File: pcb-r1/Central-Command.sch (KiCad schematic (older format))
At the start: 12 parts, among them P101 CONN_01X10, P102 CONN_01X10, P103 CONN_01X04, P104 CONN_01X02, P105 CONN_01X04, P106 CONN_01X02, U101 STM32F030C8, Y101 Crystal

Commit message: Started preliminary layout of the parts
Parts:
- C102, C103: footprint (none) -> Capacitors_SMD:C_0805
- P101, P102: footprint (none) -> Pin_Headers:Pin_Header_Straight_1x10
- P103, P105: footprint (none) -> Pin_Headers:Pin_Header_Straight_1x04
- P104, P106: footprint (none) -> Pin_Headers:Pin_Header_Straight_1x02
- Y101: footprint (none) -> Crystals:Crystal_HC49-U_Vertical
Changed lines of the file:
@@
 F 0 "Y101" H 4650 1900 50  0000 C CNN
 F 1 "Crystal" H 4650 1600 50  0000 C CNN
-F 2 "" H 4650 1750 60  0001 C CNN
+F 2 "Crystals:Crystal_HC49-U_Vertical" H 4650 1750 60  0001 C CNN
 F 3 "" H 4650 1750 60  0000 C CNN
 F 4 "http://parts.io/detail/343558/FOXSLF%2F080-20" H 4650 1750 60  0001 C CNN "Link"
@@
 F 0 "C103" V 5400 2000 50  0000 L CNN
 F 1 "20pF" V 5100 2000 50  0000 L CNN
-F 2 "" H 5288 1850 30  0001 C CNN
+F 2 "Capacitors_SMD:C_0805" H 5288 1850 30  0001 C CNN
 F 3 "" H 5250 2000 60  0000 C CNN
 	1    5250 2000
@@
 F 0 "C102" V 5400 1550 50  0000 L CNN
 F 1 "20pF" V 5100 1550 50  0000 L CNN
-F 2 "" H 5288 1400 30  0001 C CNN
+F 2 "Capacitors_SMD:C_0805" H 5288 1400 30  0001 C CNN
 F 3 "" H 5250 1550 60  0000 C CNN
 	1    5250 1550
@@
 F 0 "P101" H 700 5650 50  0000 C CNN
 F 1 "CONN_01X10" V 800 5100 50  0001 C CNN
-F 2 "" H 700 5100 60  0001 C CNN
+F 2 "Pin_Headers:Pin_Header_Straight_1x10" H 700 5100 60  0001 C CNN
 F 3 "" H 700 5100 60  0000 C CNN
 	1    700  5100
@@
 F 0 "P102" H 850 2700 50  0000 C CNN
 F 1 "CONN_01X10" V 950 2150 50  0001 C CNN
-F 2 "" H 850 2150 60  0001 C CNN
+F 2 "Pin_Headers:Pin_Header_Straight_1x10" H 850 2150 60  0001 C CNN
 F 3 "" H 850 2150 60  0000 C CNN
 	1    850  2150
@@
 F 0 "P105" H 5200 3500 50  0000 C CNN
 F 1 "CONN_01X04" V 5300 3250 50  0001 C CNN
-F 2 "" H 5200 3250 60  0001 C CNN
+F 2 "Pin_Headers:Pin_Header_Straight_1x04" H 5200 3250 60  0001 C CNN
 F 3 "" H 5200 3250 60  0000 C CNN
 	1    5200 3250
@@
 F 0 "P103" H 4950 4950 50  0000 C CNN
 F 1 "CONN_01X04" V 5050 4700 50  0001 C CNN
-F 2 "" H 4950 4700 60  0001 C CNN
+F 2 "Pin_Headers:Pin_Header_Straight_1x04" H 4950 4700 60  0001 C CNN
 F 3 "" H 4950 4700 60  0000 C CNN
 	1    4950 4700
@@
 F 0 "P106" H 6400 4850 50  0000 C CNN
 F 1 "CONN_01X02" V 6500 4700 50  0001 C CNN
-F 2 "" H 6400 4700 60  0001 C CNN
+F 2 "Pin_Headers:Pin_Header_Straight_1x02" H 6400 4700 60  0001 C CNN
 F 3 "" H 6400 4700 60  0000 C CNN
 	1    6400 4700
@@
 F 0 "P104" H 5000 6000 50  0000 C CNN
 F 1 "CONN_01X02" V 5100 5850 50  0001 C CNN
-F 2 "" H 5000 5850 60  0001 C CNN
+F 2 "Pin_Headers:Pin_Header_Straight_1x02" H 5000 5850 60  0001 C CNN
 F 3 "" H 5000 5850 60  0000 C CNN
 	1    5000 5850

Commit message: New initial layout
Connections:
- net 3V3 is gone; now on net PWR: L101.1, U101.1 (VDD), U101.24 (VDD), U101.48 (VDD)
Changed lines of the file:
@@
 	1    0    0    -1
 $EndComp
-Text GLabel 2500 900  0    60   Input ~ 0
-3V3
 Text Notes 4500 1250 0    60   ~ 0
 TODO: Get crystal/oscillator
@@
 Connection ~ 2900 3250
 Wire Wire Line
-	2500 900  2900 900
+	2250 900  2900 900
 Wire Wire Line
 	2900 800  2900 1000
@@
 Wire Wire Line
 	9450 4750 9450 5050
+Text Label 2250 900  0    60   ~ 0
+PWR
 $EndSCHEMATC

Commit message: Intermediate save of the layout
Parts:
- added C104, C107: 0.1μF, Capacitors_SMD:C_0805, symbol C
- added C105, C108: 1μF, Capacitors_SMD:C_1206, symbol C
- added C106, C109: 10μF, Capacitors_SMD:C_1206, symbol C
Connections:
- net I2C1_SLK is gone; now on net I2C1_SCK: U101.36 (PF7/I2C1_SCK)
- net GND: now also C104.1, C105.1, C106.1, C107.1, C108.1, C109.1
- net PWR: now also C104.2, C105.2, C106.2, C107.2, C108.2, C109.2
- net I2C1_SCL renamed I2C1_SCK
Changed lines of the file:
@@
 $EndComp
 $Sheet
-S 8550 1450 800  2400
+S 8550 2550 800  2400
 U 56673ABF
 F0 "Comm" 60
 F1 "Comm.sch" 60
-F2 "SWIO" I L 8550 2600 60
-F3 "SWCLK" I L 8550 2750 60
-F4 "TRACE" I L 8550 3050 60
-F5 "NRST" I L 8550 2900 60
-F6 "GND" I L 8550 1800 60
-F7 "PWR" I L 8550 1650 60
-F8 "SCL" I L 8550 2100 60
-F9 "SDA" I L 8550 2250 60
-F10 "BOOT0" I L 8550 3700 60
-F11 "MCO" I L 8550 3400 60
+F2 "SWIO" I L 8550 3700 60
+F3 "SWCLK" I L 8550 3850 60
+F4 "TRACE" I L 8550 4150 60
+F5 "NRST" I L 8550 4000 60
+F6 "GND" I L 8550 2900 60
+F7 "PWR" I L 8550 2750 60
+F8 "SCL" I L 8550 3200 60
+F9 "SDA" I L 8550 3350 60
+F10 "BOOT0" I L 8550 4800 60
+F11 "MCO" I L 8550 4500 60
 $EndSheet
-Text Label 8100 1650 0    60   ~ 0
+Text Label 8100 2750 0    60   ~ 0
 PWR
-Text Label 8100 2100 0    60   ~ 0
+Text Label 8100 3200 0    60   ~ 0
 I2C_SCL
-Text Label 8100 2250 0    60   ~ 0
+Text Label 8100 3350 0    60   ~ 0
 I2C_SDA
-Text Label 8100 2600 0    60   ~ 0
+Text Label 8100 3700 0    60   ~ 0
 SWIO
-Text Label 8100 2750 0    60   ~ 0
+Text Label 8100 3850 0    60   ~ 0
 SWCLK
-Text Label 8100 2900 0    60   ~ 0
+Text Label 8100 4000 0    60   ~ 0
 NRST
-Text Label 8100 3400 0    60   ~ 0
+Text Label 8100 4500 0    60   ~ 0
 MCO
-Text Label 8100 3700 0    60   ~ 0
+Text Label 8100 4800 0    60   ~ 0
 BOOT0
 $Sheet
-S 8250 4350 750  700
+S 8250 5450 750  700
 U 5657EAAA
 F0 "Power" 60
 F1 "Power.sch" 60
-F2 "TXD" I L 8250 4550 60
-F3 "RXD" I L 8250 4750 60
-F4 "PWR" I R 9000 4550 60
-F5 "GND" I R 9000 4750 60
+F2 "TXD" I L 8250 5650 60
+F3 "RXD" I L 8250 5850 60
+F4 "PWR" I R 9000 5650 60
+F5 "GND" I R 9000 5850 60
+F6 "NRST" I L 8250 6050 60
 $EndSheet
-Text Label 9350 4550 2    60   ~ 0
+Text Label 9350 5650 2    60   ~ 0
 PWR
 $Comp
@@
 I2C1_SDA
 Text Label 1450 2300 0    60   ~ 0
-I2C1_SLK
+I2C1_SCK
 Text Label 1450 2500 0    60   ~ 0
 BOOT0
@@
 Connection ~ 4650 2000
 Wire Wire Line
-	9000 4550 9350 4550
-Wire Wire Line
-	8550 1650 8100 1650
-Wire Wire Line
-	8550 2100 8100 2100
-Wire Wire Line
-	8550 2250 8100 2250
-Wire Wire Line
-	8550 2600 8100 2600
+	9000 5650 9350 5650
 Wire Wire Line
 	8550 2750 8100 2750
 Wire Wire Line
-	8550 2900 8100 2900
-Wire Wire Line
-	8550 3050 8100 3050
-Wire Wire Line
-	8550 3400 8100 3400
+	8550 3200 8100 3200
+Wire Wire Line
+	8550 3350 8100 3350
 Wire Wire Line
 	8550 3700 8100 3700
+Wire Wire Line
+	8550 3850 8100 3850
+Wire Wire Line
+	8550 4000 8100 4000
+Wire Wire Line
+	8550 4150 8100 4150
+Wire Wire Line
+	8550 4500 8100 4500
+Wire Wire Line
+	8550 4800 8100 4800
 Wire Wire Line
 	900  4650 2100 4650
@@
 I2C1_SDA
 Text Label 5750 5900 2    60   ~ 0
-I2C1_SCL
+I2C1_SCK
 Wire Notes Line
 	4750 5350 5900 5350
@@
 Sensor I2C Header
 Wire Wire Line
-	8250 4550 7600 4550
-Wire Wire Line
-	7600 4750 8250 4750
-Text Label 7600 4550 0    60   ~ 0
+	8250 5650 7600 5650
+Wire Wire Line
+	7600 5850 8250 5850
+Text Label 7600 5650 0    60   ~ 0
 USART2_TX
-Text Label 7600 4750 0    60   ~ 0
+Text Label 7600 5850 0    60   ~ 0
 USART2_RX
 $Comp
@@
 L GND #PWR05
 U 1 1 56673B6E
-P 9450 5050
-F 0 "#PWR05" H 9450 4800 50  0001 C CNN
-F 1 "GND" H 9450 4900 50  0000 C CNN
-F 2 "" H 9450 5050 60  0000 C CNN
-F 3 "" H 9450 5050 60  0000 C CNN
-	1    9450 5050
+P 9450 6150
+F 0 "#PWR05" H 9450 5900 50  0001 C CNN
+F 1 "GND" H 9450 6000 50  0000 C CNN
+F 2 "" H 9450 6150 60  0000 C CNN
+F 3 "" H 9450 6150 60  0000 C CNN
+	1    9450 6150
 	1    0    0    -1
 $EndComp
 Wire Wire Line
-	9000 4750 9450 4750
-Wire Wire Line
-	9450 4750 9450 5050
+	9000 5850 9450 5850
+Wire Wire Line
+	9450 5850 9450 6150
 Text Label 2250 900  0    60   ~ 0
 PWR
+Wire Wire Line
+	8250 6050 7600 6050
+Text Label 7600 6050 0    60   ~ 0
+NRST
+$Comp
+L C C104
+U 1 1 567EB894
+P 6950 1200
+F 0 "C104" H 7000 1100 50  0000 L CNN
+F 1 "0.1μF" H 6700 1300 50  0000 L CNN
+F 2 "Capacitors_SMD:C_0805" H 6988 1050 30  0001 C CNN
+F 3 "" H 6950 1200 60  0000 C CNN
+	1    6950 1200
+	-1   0    0    1
+$EndComp
+$Comp
+L C C105
+U 1 1 567EC046
+P 7400 1200
+F 0 "C105" H 7450 1100 50  0000 L CNN
+F 1 "1μF" H 7150 1300 50  0000 L CNN
+F 2 "Capacitors_SMD:C_1206" H 7438 1050 30  0001 C CNN
+F 3 "" H 7400 1200 60  0000 C CNN
+	1    7400 1200
+	-1   0    0    1
+$EndComp
+$Comp
+L C C106
+U 1 1 567EC191
+P 7800 1200
+F 0 "C106" H 7850 1100 50  0000 L CNN
+F 1 "10μF" H 7550 1300 50  0000 L CNN
+F 2 "Capacitors_SMD:C_1206" H 7838 1050 30  0001 C CNN
+F 3 "" H 7800 1200 60  0000 C CNN
+	1    7800 1200
+	-1   0    0    1
+$EndComp
+$Comp
+L C C107
+U 1 1 567ED8B8
+P 8500 1200
+F 0 "C107" H 8550 1100 50  0000 L CNN
+F 1 "0.1μF" H 8250 1300 50  0000 L CNN
+F 2 "Capacitors_SMD:C_0805" H 8538 1050 30  0001 C CNN
+F 3 "" H 8500 1200 60  0000 C CNN
+	1    8500 1200
+	-1   0    0    1
+$EndComp
+$Comp
+L C C108
+U 1 1 567ED8BE
+P 8950 1200
+F 0 "C108" H 9000 1100 50  0000 L CNN
+F 1 "1μF" H 8700 1300 50  0000 L CNN
+F 2 "Capacitors_SMD:C_1206" H 8988 1050 30  0001 C CNN
+F 3 "" H 8950 1200 60  0000 C CNN
+	1    8950 1200
+	-1   0    0    1
+$EndComp
+$Comp
+L C C109
+U 1 1 567ED8C4
+P 9350 1200
+F 0 "C109" H 9400 1100 50  0000 L CNN
+F 1 "10μF" H 9100 1300 50  0000 L CNN
+F 2 "Capacitors_SMD:C_1206" H 9388 1050 30  0001 C CNN
+F 3 "" H 9350 1200 60  0000 C CNN
+	1    9350 1200
+	-1   0    0    1
+$EndComp
+Wire Wire Line
+	6950 1050 6950 900
+Wire Wire Line
+	6950 900  9350 900
+Wire Wire Line
+	9350 900  9350 1050
+Wire Wire Line
+	9350 1350 9350 1550
+Wire Wire Line
+	9350 1550 6950 1550
+Wire Wire Line
+	6950 1550 6950 1350
+Wire Wire Line
+	7400 900  7400 1050
+Connection ~ 7400 900
+Wire Wire Line
+	7800 900  7800 1050
+Connection ~ 7800 900
+Wire Wire Line
+	8500 900  8500 1050
+Connection ~ 8500 900
+Wire Wire Line
+	8950 900  8950 1050
+Connection ~ 8950 900
+Wire Wire Line
+	8950 1350 8950 1550
+Connection ~ 8950 1550
+Wire Wire Line
+	8500 1350 8500 1550
+Connection ~ 8500 1550
+Wire Wire Line
+	7800 1350 7800 1550
+Connection ~ 7800 1550
+Wire Wire Line
+	7400 1350 7400 1550
+Wire Wire Line
+	7400 1550 7450 1550
+Connection ~ 7450 1550
+$Comp
+L GND #PWR06
+U 1 1 567EE3BC
+P 8100 1750
+F 0 "#PWR06" H 8100 1500 50  0001 C CNN
+F 1 "GND" H 8100 1600 50  0000 C CNN
+F 2 "" H 8100 1750 60  0000 C CNN
+F 3 "" H 8100 1750 60  0000 C CNN
+	1    8100 1750
+	1    0    0    -1
+$EndComp
+Wire Wire Line
+	8100 1550 8100 1750
+Connection ~ 8100 1550
+Text Label 7200 900  0    60   ~ 0
+PWR
 $EndSCHEMATC

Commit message: Final draft layout. Published to build log as V01
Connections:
- net SPI_MISO is gone; now on net SPI1_MISO: P103.3 (P3)
- net SPI_MOSI is gone; now on net SPI1_MOSI: P103.4 (P4)

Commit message: Completed the layout. Saving before sending off to Fab.
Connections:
- net MCO: now also P101.8 (P8); no longer P102.5 (P5)
- net at P101.1 (P1): now also U101.20 (PB2); no longer U101.30 (PA9)
- net at P101.2 (P2): now also U101.21 (PB10); no longer U101.31 (PA10)
- net at P101.3 (P3): now also U101.22 (PB11); no longer U101.20 (PB2)
- net at P101.5 (P5): now also U101.26 (PB13); no longer U101.21 (PB10)
- net at P101.6 (P6): now also U101.27 (PB14); no longer U101.22 (PB11)
- net at U101.25 (PB12): now also P101.4 (P4); no longer P101.7 (P7)
- net PA9: now reaches P101.9 (P9)
- net PA9: now also U101.30 (PA9); no longer U101.27 (PB14)
- net at U101.28 (PB15): now also P101.7 (P7); no longer P101.10 (P10)
- net PB8: now reaches U101.45 (PB8)
- net PB8: now also P102.5 (P5); no longer P101.4 (P4)
- new net PA10: P101.10 (P10), U101.31 (PA10)
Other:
- moved on the sheet: P101
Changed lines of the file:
@@
 L CONN_01X10 P101
 U 1 1 56677880
-P 700 5100
-F 0 "P101" H 700 5650 50  0000 C CNN
-F 1 "CONN_01X10" V 800 5100 50  0001 C CNN
-F 2 "Pin_Headers:Pin_Header_Straight_1x10" H 700 5100 60  0001 C CNN
-F 3 "" H 700 5100 60  0000 C CNN
-	1    700  5100
+P 700 5900
+F 0 "P101" H 700 6450 50  0000 C CNN
+F 1 "CONN_01X10" V 800 5900 50  0001 C CNN
+F 2 "Pin_Headers:Pin_Header_Straight_1x10" H 700 5900 60  0001 C CNN
+F 3 "" H 700 5900 60  0000 C CNN
+	1    700  5900
 	-1   0    0    -1
 $EndComp
@@
 Text Label 1450 5250 0    60   ~ 0
 SPI1_NSS
-Text Label 1450 5800 0    60   ~ 0
+Text Label 1650 5800 0    60   ~ 0
 ADC_IN8
-Text Label 1450 5900 0    60   ~ 0
+Text Label 1650 5900 0    60   ~ 0
 ADC_IN9
-Text Label 1450 6100 0    60   ~ 0
+Text Label 1650 6100 0    60   ~ 0
 SPI1_SCK
-Text Label 1450 6200 0    60   ~ 0
+Text Label 1650 6200 0    60   ~ 0
 SPI1_MISO
-Text Label 1450 6300 0    60   ~ 0
+Text Label 1650 6300 0    60   ~ 0
 SPI1_MOSI
-Text Label 1450 6400 0    60   ~ 0
+Text Label 1650 6400 0    60   ~ 0
 USART1_TX
-Text Label 1450 6500 0    60   ~ 0
+Text Label 1650 6500 0    60   ~ 0
 USART1_RX
-Text Label 1450 6700 0    60   ~ 0
+Text Label 1650 6700 0    60   ~ 0
 PB9
 Text Label 1450 2200 0    60   ~ 0
@@
 Text Label 1300 2000 2    60   ~ 0
 PB9
-Text Label 1300 2100 2    60   ~ 0
+Text Label 1200 6150 2    60   ~ 0
 MCO
 Text Label 1450 3850 0    60   ~ 0
@@
 Text Label 7200 900  0    60   ~ 0
 PWR
+Text Label 1450 4650 0    60   ~ 0
+PA9
+Text Label 1450 4750 0    60   ~ 0
+PA10
+Text Label 1200 6250 2    60   ~ 0
+PA9
+Text Label 1200 6350 2    60   ~ 0
+PA10
+Text Label 1650 6600 0    60   ~ 0
+PB8
+Text Label 1300 2100 2    60   ~ 0
+PB8
 Wire Wire Line
 	2950 800  2900 800
@@
 	8550 4800 8100 4800
 Wire Wire Line
-	900  4650 2100 4650
-Wire Wire Line
-	900  4750 2100 4750
-Wire Wire Line
 	2100 4850 1450 4850
 Wire Wire Line
@@
 	2100 5250 1450 5250
 Wire Wire Line
-	900  4850 1400 4850
-Wire Wire Line
-	1400 4850 1400 6000
-Wire Wire Line
-	1400 6000 2100 6000
-Wire Wire Line
-	900  4950 1350 4950
-Wire Wire Line
-	1350 4950 1350 6600
-Wire Wire Line
-	1350 6600 2100 6600
-Wire Wire Line
-	900  5050 1300 5050
-Wire Wire Line
-	1300 5050 1300 6800
-Wire Wire Line
-	1300 6800 2100 6800
-Wire Wire Line
-	900  5150 1250 5150
-Wire Wire Line
-	1250 5150 1250 6900
-Wire Wire Line
-	1250 6900 2100 6900
-Wire Wire Line
-	900  5250 1200 5250
-Wire Wire Line
-	1200 5250 1200 7000
-Wire Wire Line
-	1200 7000 2100 7000
-Wire Wire Line
-	900  5350 1150 5350
-Wire Wire Line
-	1150 5350 1150 7100
-Wire Wire Line
-	1150 7100 2100 7100
-Wire Wire Line
-	900  5450 1100 5450
-Wire Wire Line
-	1100 5450 1100 7200
-Wire Wire Line
-	1100 7200 2100 7200
-Wire Wire Line
-	900  5550 1050 5550
-Wire Wire Line
-	1050 5550 1050 7300
-Wire Wire Line
-	1050 7300 2100 7300
-Wire Wire Line
-	2100 5800 1450 5800
-Wire Wire Line
-	2100 6100 1450 6100
-Wire Wire Line
-	2100 6200 1450 6200
-Wire Wire Line
-	2100 6300 1450 6300
-Wire Wire Line
-	2100 6500 1450 6500
-Wire Wire Line
-	2100 6400 1450 6400
-Wire Wire Line
-	2100 6700 1450 6700
-Wire Wire Line
-	2100 5900 1450 5900
+	1600 6000 2100 6000
+Wire Wire Line
+	900  5550 1500 5550
+Wire Wire Line
+	1500 5550 1500 6800
+Wire Wire Line
+	1500 6800 2100 6800
+Wire Wire Line
+	900  5650 1450 5650
+Wire Wire Line
+	1450 5650 1450 6900
+Wire Wire Line
+	1450 6900 2100 6900
+Wire Wire Line
+	900  5750 1400 5750
+Wire Wire Line
+	1400 5750 1400 7000
+Wire Wire Line
+	1400 7000 2100 7000
+Wire Wire Line
+	900  5850 1350 5850
+Wire Wire Line
+	1350 5850 1350 7100
+Wire Wire Line
+	1350 7100 2100 7100
+Wire Wire Line
+	900  5950 1300 5950
+Wire Wire Line
+	1300 5950 1300 7200
+Wire Wire Line
+	1300 7200 2100 7200
+Wire Wire Line
+	900  6050 1250 6050
+Wire Wire Line
+	1250 6050 1250 7300
+Wire Wire Line
+	1250 7300 2100 7300
+Wire Wire Line
+	2100 5800 1650 5800
+Wire Wire Line
+	2100 6100 1650 6100
+Wire Wire Line
+	2100 6200 1650 6200
+Wire Wire Line
+	2100 6300 1650 6300
+Wire Wire Line
+	2100 6500 1650 6500
+Wire Wire Line
+	2100 6400 1650 6400
+Wire Wire Line
+	2100 6700 1650 6700
+Wire Wire Line
+	2100 5900 1650 5900
 Wire Wire Line
 	2100 2650 1450 2650
@@
 	8100 1750 8100 1600
 Connection ~ 8100 1600
+Wire Wire Line
+	2100 4650 1450 4650
+Wire Wire Line
+	2100 4750 1450 4750
+Wire Wire Line
+	900  6150 1200 6150
+Wire Wire Line
+	900  6250 1200 6250
+Wire Wire Line
+	2100 6600 1650 6600
+Wire Wire Line
+	900  5450 1600 5450
+Wire Wire Line
+	900  6350 1200 6350
+Wire Wire Line
+	1600 5450 1600 6000
 $EndSCHEMATC

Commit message: Preparing the BOM
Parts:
- C101: value C -> 0.1μF
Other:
- note added: "TODO - Verify the value of C101"
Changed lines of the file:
@@
 P 4000 1050
 F 0 "C101" H 4025 1150 50  0000 L CNN
-F 1 "C" H 4025 950 50  0000 L CNN
+F 1 "0.1μF" H 4025 950 50  0000 L CNN
 F 2 "Capacitors_SMD:C_0805" H 4038 900 30  0001 C CNN
 F 3 "" H 4000 1050 60  0000 C CNN
@@
 Wire Wire Line
 	1600 5450 1600 6000
+Text Notes 3830 790  0    60   ~ 0
+TODO - Verify the value of C101
 $EndSCHEMATC

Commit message: Added the MPN for the crystal
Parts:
- Y101: MPN (none) -> FOXSLF/080-20
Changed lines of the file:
@@
 F 3 "" H 4650 1750 60  0000 C CNN
 F 4 "http://parts.io/detail/343558/FOXSLF%2F080-20" H 4650 1750 60  0001 C CNN "Link"
+F 5 "FOXSLF/080-20" H 4650 1750 60  0001 C CNN "MPN"
 	1    4650 1750
 	0    1    1    0

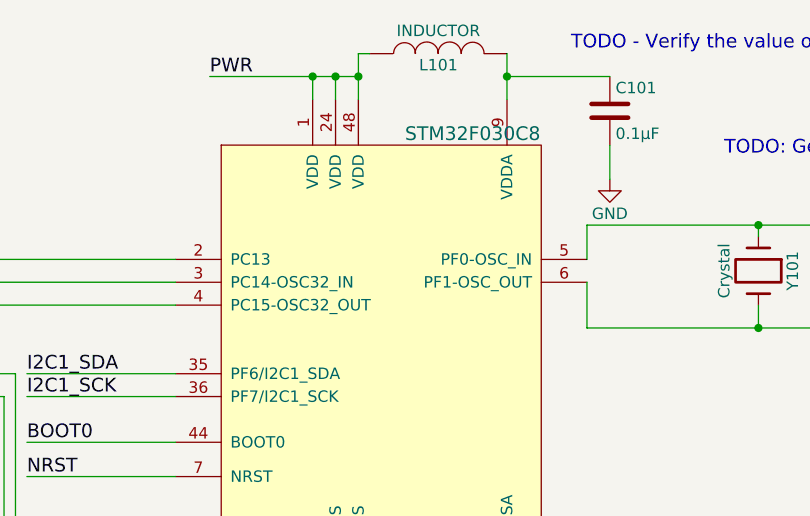
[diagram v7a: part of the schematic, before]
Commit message: Updated the parts for the BOM
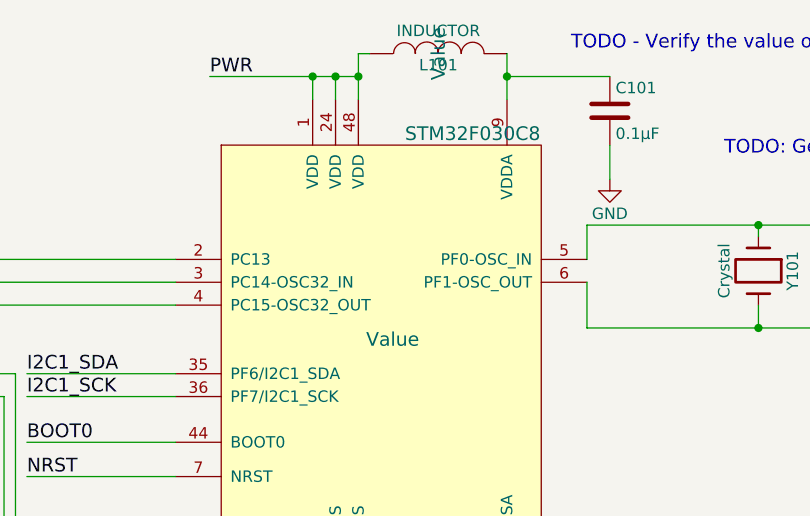
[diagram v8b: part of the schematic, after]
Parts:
- L101: ConradPN (none) -> Value; DigiKeyPN (none) -> 490-6588-1-ND; Label (none) -> Value; MPN (none) -> LQH31CN100K03L
- U101: ConradPN (none) -> Value; DigiKeyPN (none) -> 497-14043-ND; Label (none) -> Value; MPN (none) -> STM32F030C8
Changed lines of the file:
@@
 F 2 "Housings_QFP:LQFP-48_7x7mm_Pitch0.5mm" H 3050 2050 60  0001 C CNN
 F 3 "" H 3050 2050 60  0000 C CNN
+F 4 "STM32F030C8" H 3050 2050 60  0001 C CNN "MPN"
+F 5 "Value" H 3050 2050 60  0001 C CNN "ConradPN"
+F 6 "Value" H 3050 2050 60  0000 C CNN "Label"
+F 7 "497-14043-ND" H 3050 2050 60  0001 C CNN "DigiKeyPN"
 	3    3050 2050
 	1    0    0    -1
@@
 F 2 "Inductors_NEOSID:Neosid_Inductor_SM1206" H 3250 800 60  0001 C CNN
 F 3 "" H 3250 800 60  0000 C CNN
+F 4 "LQH31CN100K03L" H 3250 800 60  0001 C CNN "MPN"
+F 5 "Value" H 3250 800 60  0001 C CNN "ConradPN"
+F 6 "Value" H 3250 800 60  0000 C CNN "Label"
+F 7 "490-6588-1-ND" V 3250 800 60  0001 C CNN "DigiKeyPN"
 	1    3250 800
 	0    -1   -1   0
